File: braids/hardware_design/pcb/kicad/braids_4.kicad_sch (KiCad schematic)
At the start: 16 parts

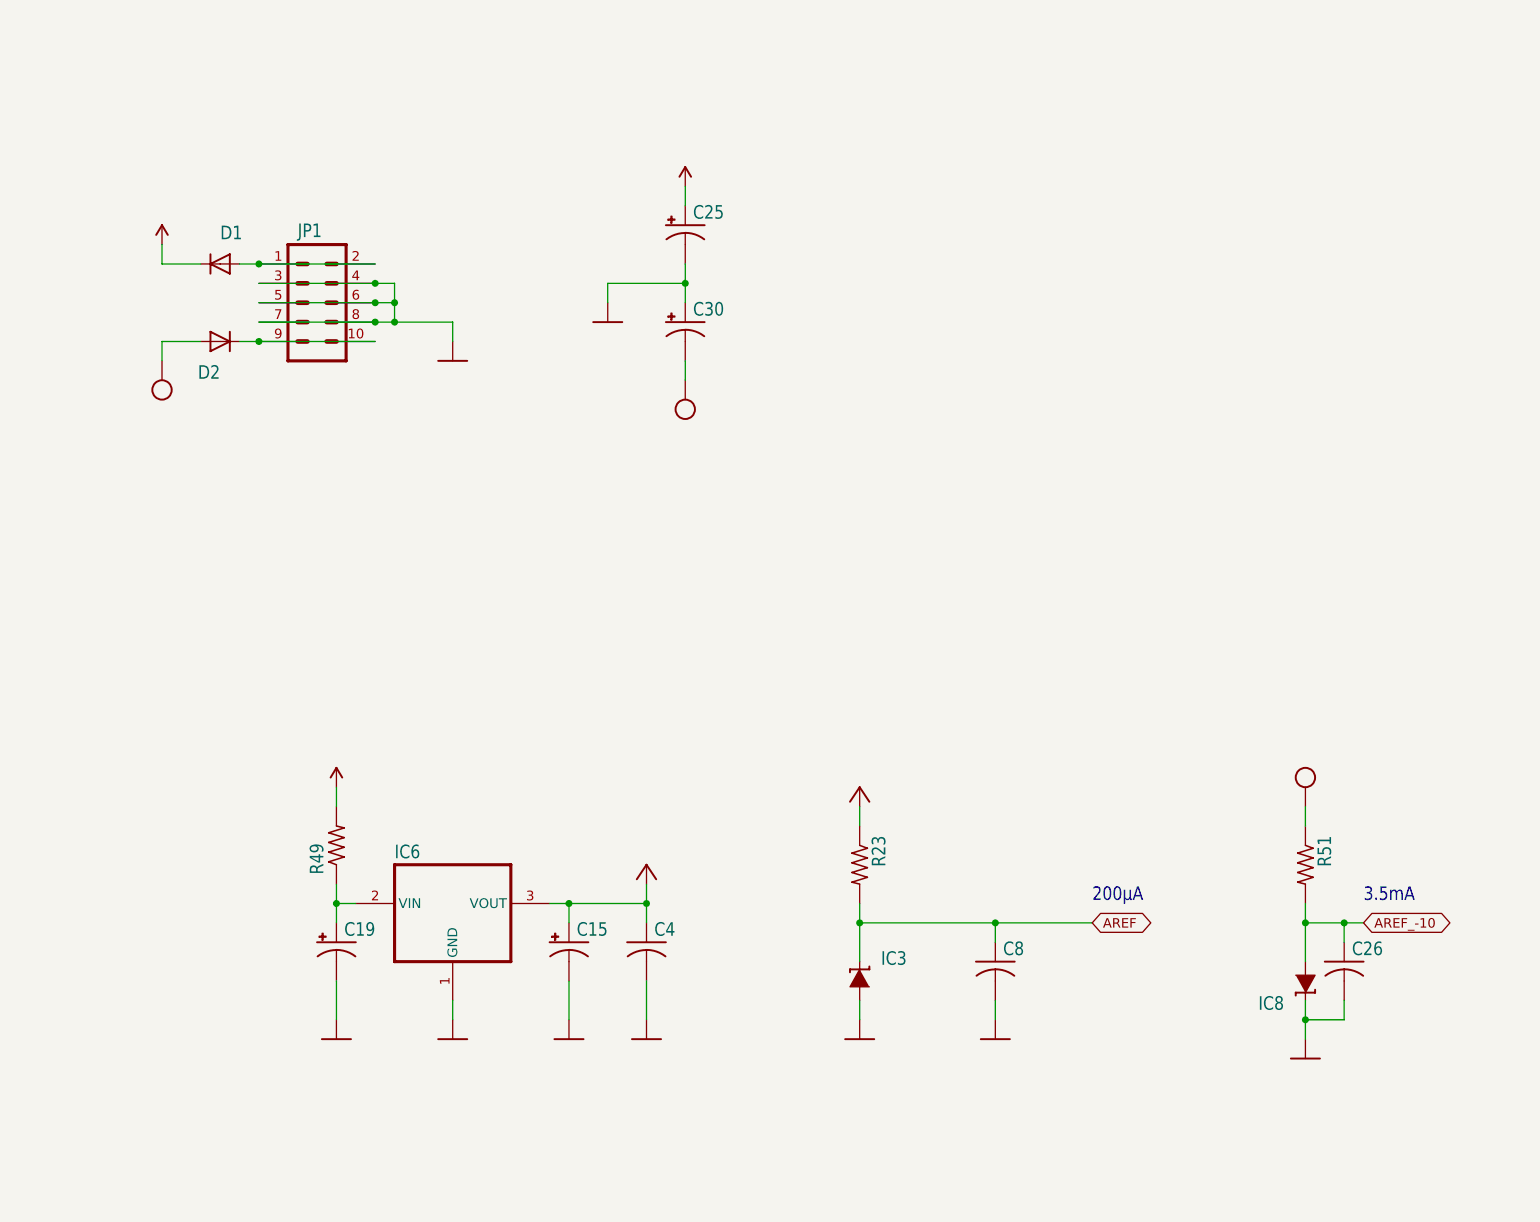
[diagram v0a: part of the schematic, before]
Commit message: changed mcp3204 to mcp3208
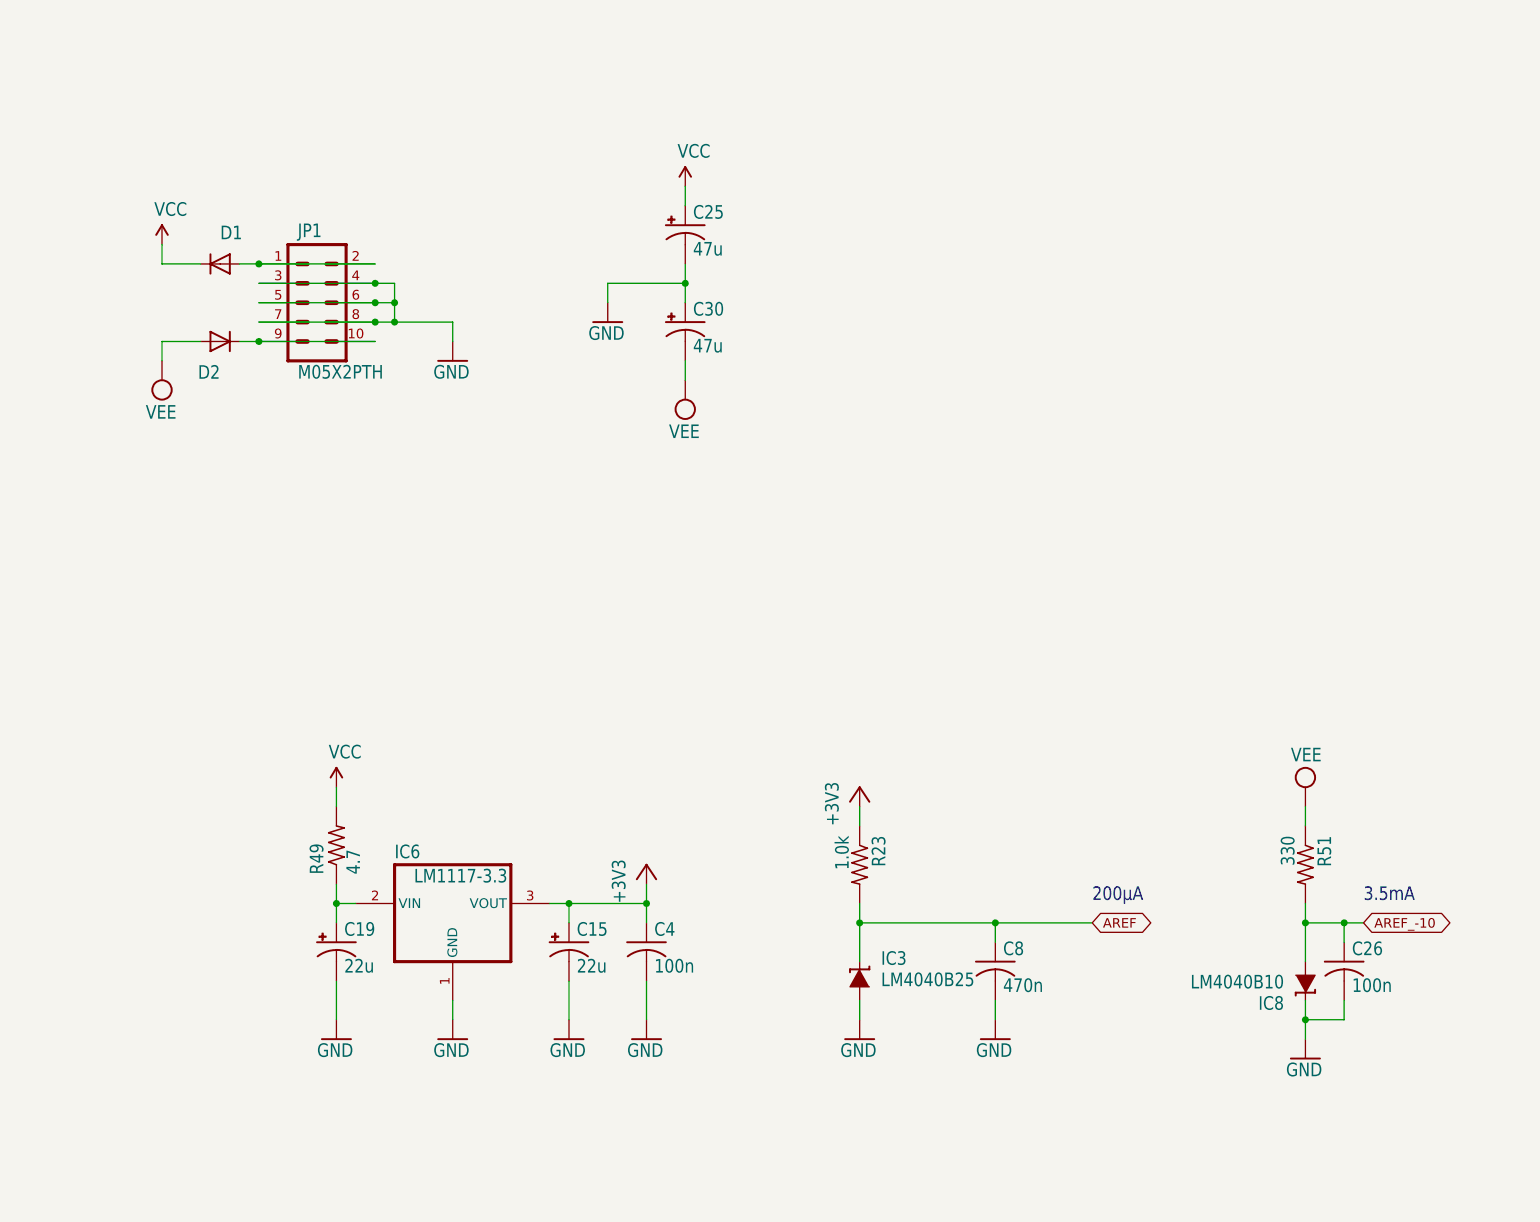
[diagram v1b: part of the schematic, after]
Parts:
- C15, C19: value (none) -> 22u; footprint (none) -> braids:PANASONIC_C
- C25, C30: value (none) -> 47u; footprint (none) -> braids:PANASONIC_D
- C26, C4: value (none) -> 100n; footprint (none) -> braids:C0603
- C8: value (none) -> 470n; footprint (none) -> braids:C0603
- D1, D2: value (none) -> 1N5819HW; footprint (none) -> braids:SOD123
- IC3: value (none) -> LM4040B25; footprint (none) -> braids:DBZ_R-PDSO-G3
- IC6: value (none) -> LM1117-3.3; footprint (none) -> braids:TO252
- IC8: value (none) -> LM4040B10; footprint (none) -> braids:DBZ_R-PDSO-G3
- JP1: value (none) -> M05X2PTH; footprint (none) -> braids:AVR_ICSP
- R23: value (none) -> 1.0k; footprint (none) -> braids:R0603
- R49: value (none) -> 4.7; footprint (none) -> braids:R1206
- R51: value (none) -> 330; footprint (none) -> braids:R0603
